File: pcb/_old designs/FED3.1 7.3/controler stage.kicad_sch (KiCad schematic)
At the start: 25 parts, among them IC4 RTC PCF8523T, J1 Conn_02x03_Odd_Even, SW2 SPST_TACT-KMR2, U1 ATSAMD21G18A, U4 Adafruit LCD Screen, X1 ClockXtal, X2 uXtal, X4 microsd

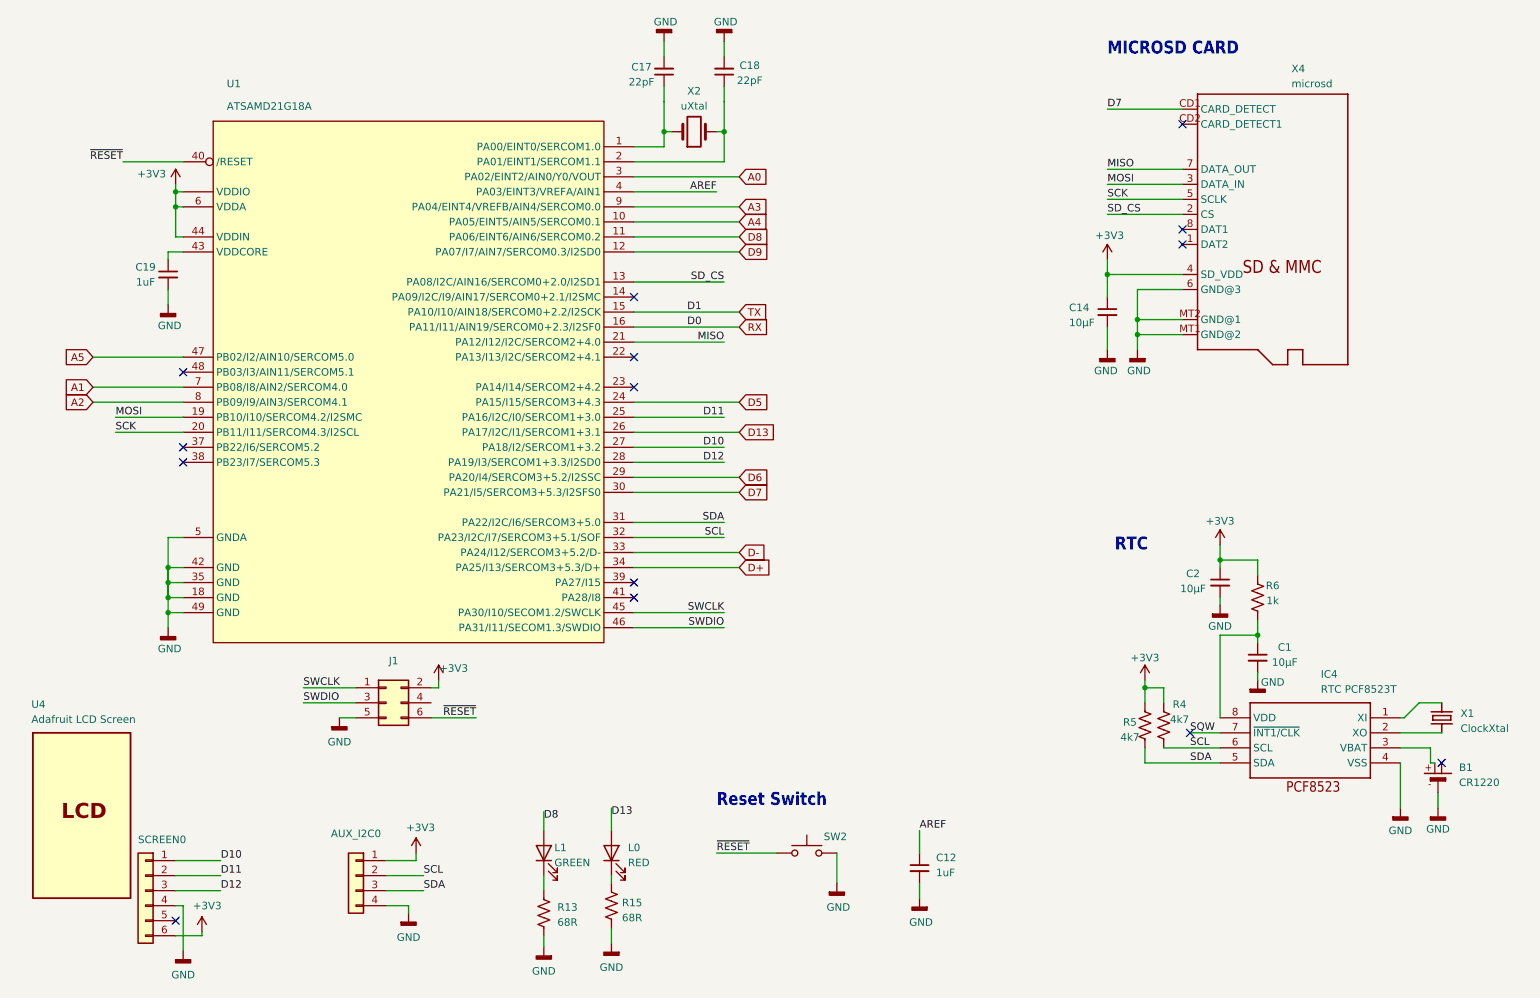
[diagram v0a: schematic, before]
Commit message: v.7.4 - alterações rail power
v.7.4
- modificada estrutura rail power: VUSB apenas para Vcharging
- modificadas Rs de LEDs para diminuir I
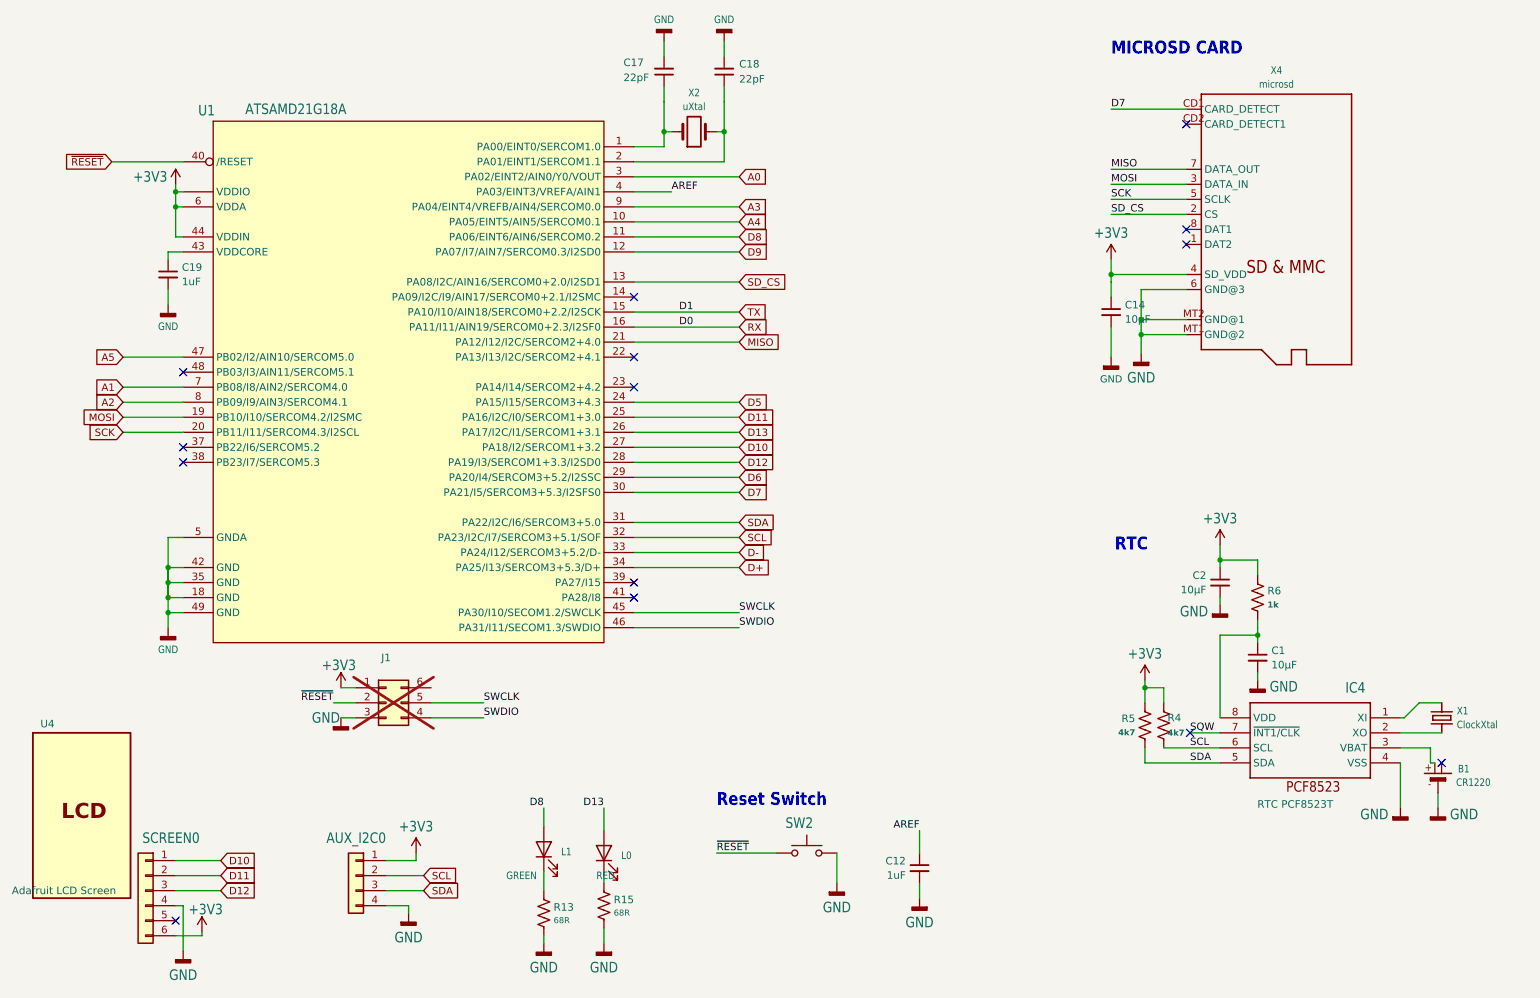
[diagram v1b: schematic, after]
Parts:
- AUX_I2C0: footprint FED3_PCBLib:1X04 -> FED3_v7.3:1X04
- B1: footprint FED3_PCBLib:CR1220 -> FED3_v7.3:CR1220; symbol FED3 SymbLib:BATTERYCR1220_SMT -> FED3_v7.3 SymLib:BATTERYCR1220_SMT
- IC4: symbol FED3 SymbLib:RTC_PCF8523/TK -> FED3_v7.3 SymLib:RTC_PCF8523/TK
- J1: value Conn_02x03_Odd_Even -> Conn_06Pins; symbol Connector_Generic:Conn_02x03_Odd_Even -> Connector_Generic:Conn_02x03_Counter_Clockwise; MPN PR20203VBDN -> 67996-206HLF; OEPSPN OEPS070124 -> OEPS070015; now not fitted; now left out of the parts list
- L0: MPN 5975004407F -> VFHR1116P-4C82A-TR; OEPSPN OEPS030006 -> OEPS030038
- L1: MPN 150060VS75000 -> LTST-C191KGKT
- SCREEN0: footprint FED3_PCBLib:1X06 -> FED3_v7.3:1X06
- U1: footprint FED3_PCBLib:TQFN48_7MM -> FED3_v7.3:TQFN48_7MM; symbol FED3 SymbLib:ATSAMD21J_QFN -> FED3_v7.3 SymLib:ATSAMD21J_QFN
- U4: footprint (none) -> -; symbol FED3 SymbLib:LCD_SCREEN -> FED3_v7.3 SymLib:LCD_SCREEN; OEPSPN TBD -> waiting...
- X1: footprint FED3_PCBLib:CRYSTAL_8X3.8 -> FED3_v7.3:CRYSTAL_8X3.8; symbol FED3 SymbLib:CRYSTAL8.0X3.8 -> FED3_v7.3 SymLib:CRYSTAL8.0X3.8
- X2: footprint Crystal:Crystal_SMD_MicroCrystal_CC8V-T1A-2Pin_2.0x1.2mm -> Crystal:Crystal_SMD_MicroCrystal_CC7V-T1A-2Pin_3.2x1.5mm
- X4: footprint FED3_PCBLib:MICROSD -> FED3_v7.3:MICROSD; symbol FED3 SymbLib:MICROSD -> FED3_v7.3 SymLib:MICROSD
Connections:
- net +3V3: now also J1.1 (Pin_1); no longer J1.2 (Pin_2)
- net GND: now also J1.3 (Pin_3); no longer J1.5 (Pin_5)
- net SWCLK: now also J1.5 (Pin_5); no longer J1.1 (Pin_1)
- net SWDIO: now also J1.4 (Pin_4); no longer J1.3 (Pin_3)
- net ~{RESET}: now also J1.2 (Pin_2); no longer J1.6 (Pin_6)
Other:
- moved on the sheet: C14, L0, L1, R15, X4
